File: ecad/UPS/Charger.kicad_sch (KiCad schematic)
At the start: 70 parts, among them J1 Barrel_Jack, J2 Conn_01x02_Pin, J5 Conn_01x02_Pin, J6 Conn_01x02_Pin, Q1 CSD18540Q5B, Q2 Q_PMOS_DGS, Q4 Q_PMOS_DGS, Q5 CSD18540Q5B, Q6 CSD18540Q5B, Q7 CSD18540Q5B, U1 BQ25730RSNR

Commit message: Started GND consolidation
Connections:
- net GND: now also C1.2, C2.2, C28.1, C29.1, C30.1, C31.1, C38.2, R1.2, R2.2, R3.2
- net GNDA: no longer C1.2, C2.2, C28.1, C29.1, C30.1, C31.1, C38.2, R1.2, R2.2, R3.2
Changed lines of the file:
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@@
 	(global_label "REGN"
 		(shape input)
-		(at 257.81 152.4 90)
+		(at 257.81 152.4 0)
 		(fields_autoplaced yes)
 		(effects
@@
 		)
 		(property "Intersheetrefs" "${INTERSHEET_REFS}"
-			(at 257.81 144.3953 90)
+			(at 265.8147 152.4 0)
 			(hide yes)
 			(show_name no)
@@
 			)
 		)
-		(property "Value" "GNDA"
-			(at 146.05 242.5699 90)
+		(property "Value" "GND"
+			(at 148.59 238.76 90)
 			(show_name no)
 			(do_not_autoplace no)
@@
 					(size 1.27 1.27)
 				)
-				(justify right)
 			)
 		)
@@
 			)
 		)
-		(property "Value" "GNDA"
+		(property "Value" "GND"
 			(at 102.87 163.8299 90)
 			(show_name no)
@@
 			)
 		)
-		(property "Value" "GNDA"
-			(at 260.35 201.93 0)
+		(property "Value" "GND"
+			(at 262.89 198.1199 0)
 			(show_name no)
 			(do_not_autoplace no)
@@
 					(size 1.27 1.27)
 				)
+				(justify left)
 			)
 		)
@@
 			)
 		)
-		(property "Value" "GNDA"
-			(at 243.84 203.2 0)
+		(property "Value" "GND"
+			(at 246.38 199.3899 0)
 			(show_name no)
 			(do_not_autoplace no)
@@
 					(size 1.27 1.27)
 				)
+				(justify left)
 			)
 		)
@@
 			)
 		)
-		(property "Value" "GNDA"
-			(at 102.87 177.7999 90)
+		(property "Value" "GND"
+			(at 105.41 173.99 90)
 			(show_name no)
 			(do_not_autoplace no)
@@
 					(size 1.27 1.27)
 				)
-				(justify right)
 			)
 		)
@@
 			)
 		)
-		(property "Value" "GNDA"
-			(at 250.19 201.93 0)
+		(property "Value" "GND"
+			(at 252.73 198.1199 0)
 			(show_name no)
 			(do_not_autoplace no)
@@
 					(size 1.27 1.27)
 				)
+				(justify left)
 			)
 		)
@@
 			)
 		)
-		(property "Value" "GNDA"
+		(property "Value" "GND"
 			(at 273.05 203.2 0)
 			(show_name no)

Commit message: Rename all grounds to GND
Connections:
- net GND: now also C68.2, C69.2, C70.2, J2.2 (Pin_2), J5.2 (Pin_2), J6.2 (Pin_2)
- net GNDA: no longer C68.2, C69.2, C70.2, J2.2 (Pin_2), J5.2 (Pin_2), J6.2 (Pin_2)

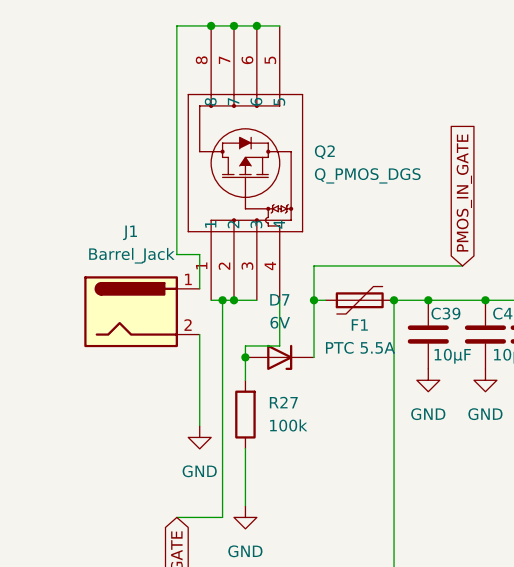
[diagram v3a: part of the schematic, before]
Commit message: Little routing, also fixed barrel jack to match input
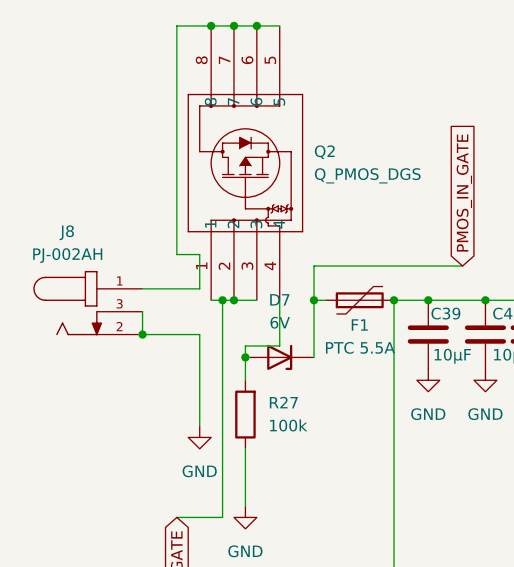
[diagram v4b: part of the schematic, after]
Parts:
- removed J1: Barrel_Jack, Connector_BarrelJack:BarrelJack_Horizontal, symbol Connector:Barrel_Jack
- added J8: PJ-002AH, PJ-002AH:CUI_PJ-002AH, symbol PJ-002AH:PJ-002AH
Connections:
- net GND: now also J8.2, J8.3
- net at Q2.5, Q2.6, Q2.7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: now also J8.1
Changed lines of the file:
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@@
 	)
 	(junction
+		(at 92.71 87.63)
+		(diameter 0)
+		(color 0 0 0 0)
+	)
+	(junction
 		(at 321.31 95.25)
 		(diameter 0)
@@
 	(wire
 		(pts
+			(xy 92.71 85.09) (xy 92.71 87.63)
+		)
+		(stroke
+			(width 0)
+			(type default)
+		)
+	)
+	(wire
+		(pts
 			(xy 104.14 90.17) (xy 104.14 92.71)
 		)
@@
 	(wire
 		(pts
+			(xy 92.71 87.63) (xy 99.06 87.63)
+		)
+		(stroke
+			(width 0)
+			(type default)
+		)
+	)
+	(wire
+		(pts
 			(xy 273.05 177.8) (xy 273.05 185.42)
 		)
@@
 	(wire
 		(pts
+			(xy 92.71 82.55) (xy 99.06 82.55)
+		)
+		(stroke
+			(width 0)
+			(type default)
+		)
+	)
+	(wire
+		(pts
 			(xy 101.6 83.82) (xy 102.87 83.82)
 		)
@@
 	)
 	(symbol
+		(lib_id "PJ-002AH:PJ-002AH")
+		(at 87.63 85.09 0)
+		(unit 1)
+		(body_style 1)
+		(exclude_from_sim no)
+		(in_bom yes)
+		(on_board yes)
+		(in_pos_files yes)
+		(dnp no)
+		(fields_autoplaced yes)
+		(property "Reference" "J8"
+			(at 84.3943 76.2 0)
+			(show_name no)
+			(do_not_autoplace no)
+			(effects
+				(font
+					(size 1.27 1.27)
+				)
+			)
+		)
+		(property "Value" "PJ-002AH"
+			(at 84.3943 78.74 0)
+			(show_name no)
+			(do_not_autoplace no)
+			(effects
+				(font
+					(size 1.27 1.27)
+				)
+			)
+		)
+		(property "Footprint" "PJ-002AH:CUI_PJ-002AH"
+			(at 87.63 85.09 0)
+			(hide yes)
+			(show_name no)
+			(do_not_autoplace no)
+			(effects
+				(font
+					(size 1.27 1.27)
+				)
+				(justify bottom)
+			)
+		)
+		(property "Datasheet" ""
+			(at 87.63 85.09 0)
+			(hide yes)
+			(show_name no)
+			(do_not_autoplace no)
+			(effects
+				(font
+					(size 1.27 1.27)
+				)
+			)
+		)
+		(property "Description" "Power Barrel Connector Jack 2.10mm ID (0.083), 5.50mm OD (0.217) Through Hole, Right Angle"
+			(at 87.63 85.09 0)
+			(hide yes)
+			(show_name no)
+			(do_not_autoplace no)
+			(effects
+				(font
+					(size 1.27 1.27)
+				)
+				(justify bottom)
+			)
+		)
+		(property "MF" "Same Sky"
+			(at 87.63 85.09 0)
+			(hide yes)
+			(show_name no)
+			(do_not_autoplace no)
+			(effects
+				(font
+					(size 1.27 1.27)
+				)
+				(justify bottom)
+			)
+		)
+		(property "Package" "None"
+			(at 87.63 85.09 0)
+			(hide yes)
+			(show_name no)
+			(do_not_autoplace no)
+			(effects
+				(font
+					(size 1.27 1.27)
+				)
+				(justify bottom)
+			)
+		)
+		(property "Price" "None"
+			(at 87.63 85.09 0)
+			(hide yes)
+			(show_name no)
+			(do_not_autoplace no)
+			(effects
+				(font
+					(size 1.27 1.27)
+				)
+				(justify bottom)
+			)
+		)
+		(property "Check_prices" "https://www.snapeda.com/parts/PJ-002AH/Same+Sky/view-part/?ref=eda"
+			(at 87.63 85.09 0)
+			(hide yes)
+			(show_name no)
+			(do_not_autoplace no)
+			(effects
+				(font
+					(size 1.27 1.27)
+				)
+				(justify bottom)
+			)
+		)
+		(property "STANDARD" "Manufacturer recommendations"
+			(at 87.63 85.09 0)
+			(hide yes)
+			(show_name no)
+			(do_not_autoplace no)
+			(effects
+				(font
+					(size 1.27 1.27)
+				)
+				(justify bottom)
+			)
+		)
+		(property "SnapEDA_Link" "https://www.snapeda.com/parts/PJ-002AH/Same+Sky/view-part/?ref=snap"
+			(at 87.63 85.09 0)
+			(hide yes)
+			(show_name no)
+			(do_not_autoplace no)
+			(effects
+				(font
+					(size 1.27 1.27)
+				)
+				(justify bottom)
+			)
+		)
+		(property "MP" "PJ-002AH"
+			(at 87.63 85.09 0)
+			(hide yes)
+			(show_name no)
+			(do_not_autoplace no)
+			(effects
+				(font
+					(size 1.27 1.27)
+				)
+				(justify bottom)
+			)
+		)
+		(property "Purchase-URL" "https://www.snapeda.com/api/url_track_click_mouser/?unipart_id=448876&manufacturer=Same Sky&part_name=PJ-002AH&search_term=pj-002ah"
+			(at 87.63 85.09 0)
+			(hide yes)
+			(show_name no)
+			(do_not_autoplace no)
+			(effects
+				(font
+					(size 1.27 1.27)
+				)
+				(justify bottom)
+			)
+		)
+		(property "Availability" "In Stock"
+			(at 87.63 85.09 0)
+			(hide yes)
+			(show_name no)
+			(do_not_autoplace no)
+			(effects
+				(font
+					(size 1.27 1.27)
+				)
+				(justify bottom)
+			)
+		)
+		(property "MANUFACTURER" "CUI INC"
+			(at 87.63 85.09 0)
+			(hide yes)
+			(show_name no)
+			(do_not_autoplace no)
+			(effects
+				(font
+					(size 1.27 1.27)
+				)
+				(justify bottom)
+			)
+		)
+		(pin "1"
+		)
+		(pin "2"
+		)
+		(pin "3"
+		)
+		(instances
+			(project "UPS"
+				(path "/9d92b60a-4a6b-449c-b462-cab19e69d38c/58e8621a-e50a-4c31-8927-fd6b72ccb3ce"
+					(reference "J8")
+					(unit 1)
+				)
+			)
+		)
+	)
+	(symbol
 		(lib_id "Device:C")
 		(at 330.2 88.9 0)
@@
 					(unit 1)
 				)
-			)
-		)
-	)
-	(symbol
-		(lib_id "Connector:Barrel_Jack")
-		(at 91.44 85.09 0)
-		(unit 1)
-		(body_style 1)
-		(exclude_from_sim no)
-		(in_bom yes)
-		(on_board yes)
-		(in_pos_files yes)
-		(dnp no)
-		(fields_autoplaced yes)
-		(property "Reference" "J1"
-			(at 91.44 76.2 0)
-			(show_name no)
-			(do_not_autoplace no)
-			(effects
-				(font
-					(size 1.27 1.27)
-				)
-			)
-		)
-		(property "Value" "Barrel_Jack"
-			(at 91.44 78.74 0)
-			(show_name no)
-			(do_not_autoplace no)
-			(effects
-				(font
-					(size 1.27 1.27)
-				)
-			)
-		)
-		(property "Footprint" "Connector_BarrelJack:BarrelJack_Horizontal"
-			(at 92.71 86.106 0)
-			(hide yes)
-			(show_name no)
-			(do_not_autoplace no)
-			(effects
-				(font
-					(size 1.27 1.27)
-				)
-			)
-		)
-		(property "Datasheet" ""
-			(at 92.71 86.106 0)
-			(hide yes)
-			(show_name no)
-			(do_not_autoplace no)
-			(effects
-				(font
-					(size 1.27 1.27)
-				)
-			)
-		)
-		(property "Description" "DC Barrel Jack"
-			(at 91.44 85.09 0)
-			(hide yes)
-			(show_name no)
-			(do_not_autoplace no)
-			(effects
-				(font
-					(size 1.27 1.27)
-				)
-			)
-		)
-		(pin "1"
-		)
-		(pin "2"
-		)
-		(instances
-			(project "Charger"
-				(path "/58c05fa3-b10b-4b83-957c-b8220bb8f680"
-					(reference "J1")
-					(unit 1)
-				)
-			)
-			(project "UPS"
-				(path "/9d92b60a-4a6b-449c-b462-cab19e69d38c/58e8621a-e50a-4c31-8927-fd6b72ccb3ce"
-					(reference "J1")
-					(unit 1)
-				)

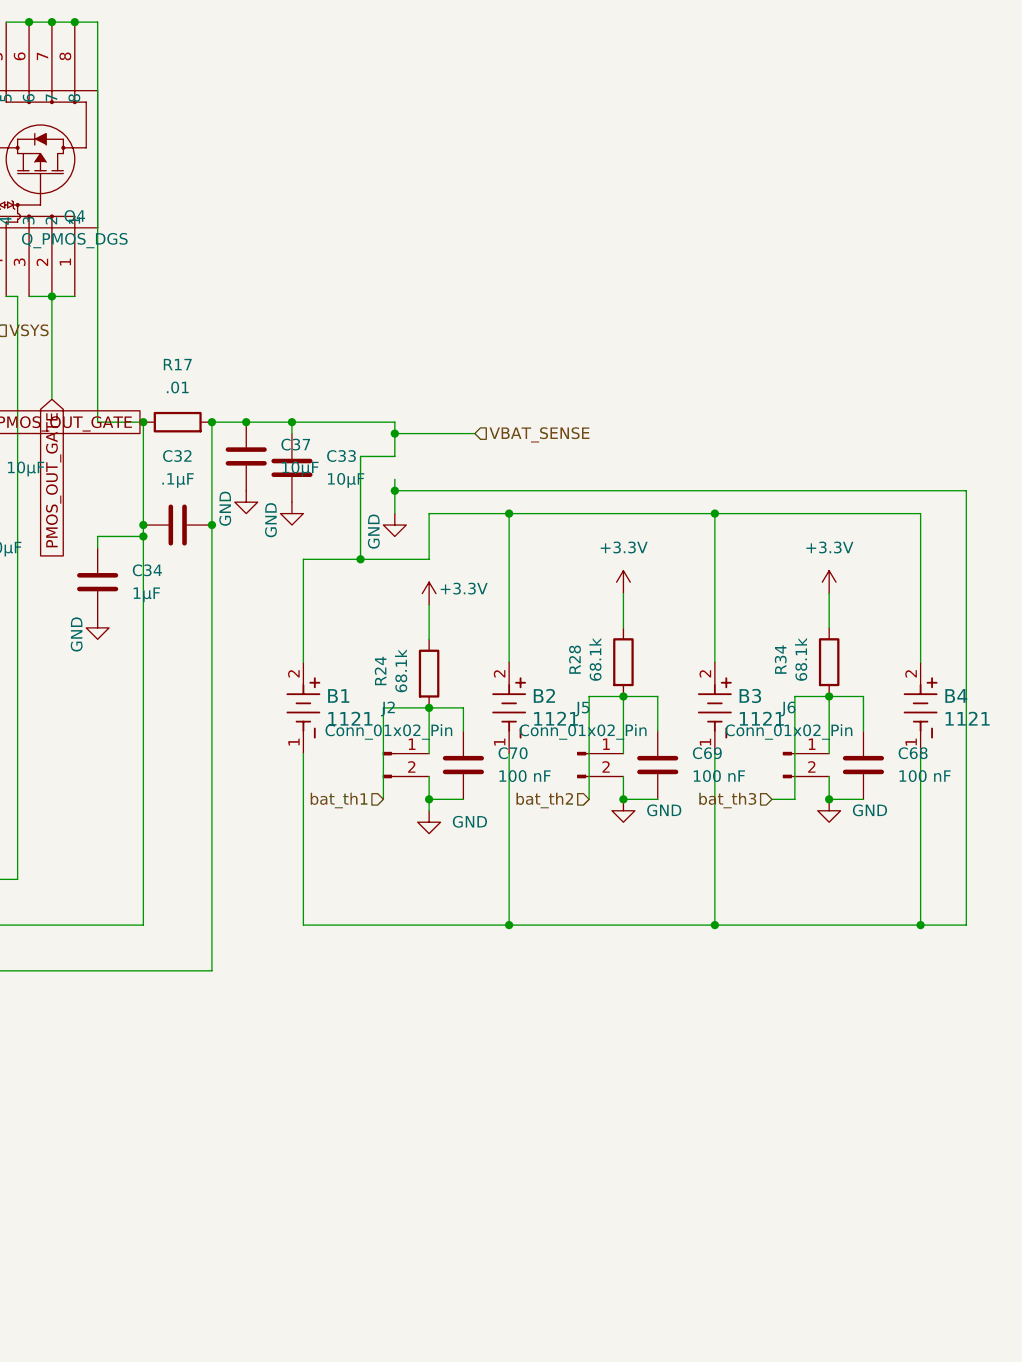
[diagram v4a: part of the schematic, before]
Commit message: touches
Add battery and board thermistor circuits on PC0/PC1.

Implement ADC sampling, temperature conversion, and sensor fault reporting.

Enable the STM32 ADC drivers and poll temperatures in the main loop.

Add the OLED connector on PB10/PB11 and update PCB footprints and net assignments.

Add a Raspberry Pi mounting-hole footprint.

Exclude local docs and test folders from Git.

five ADC sensor inputs

fan-control logic.
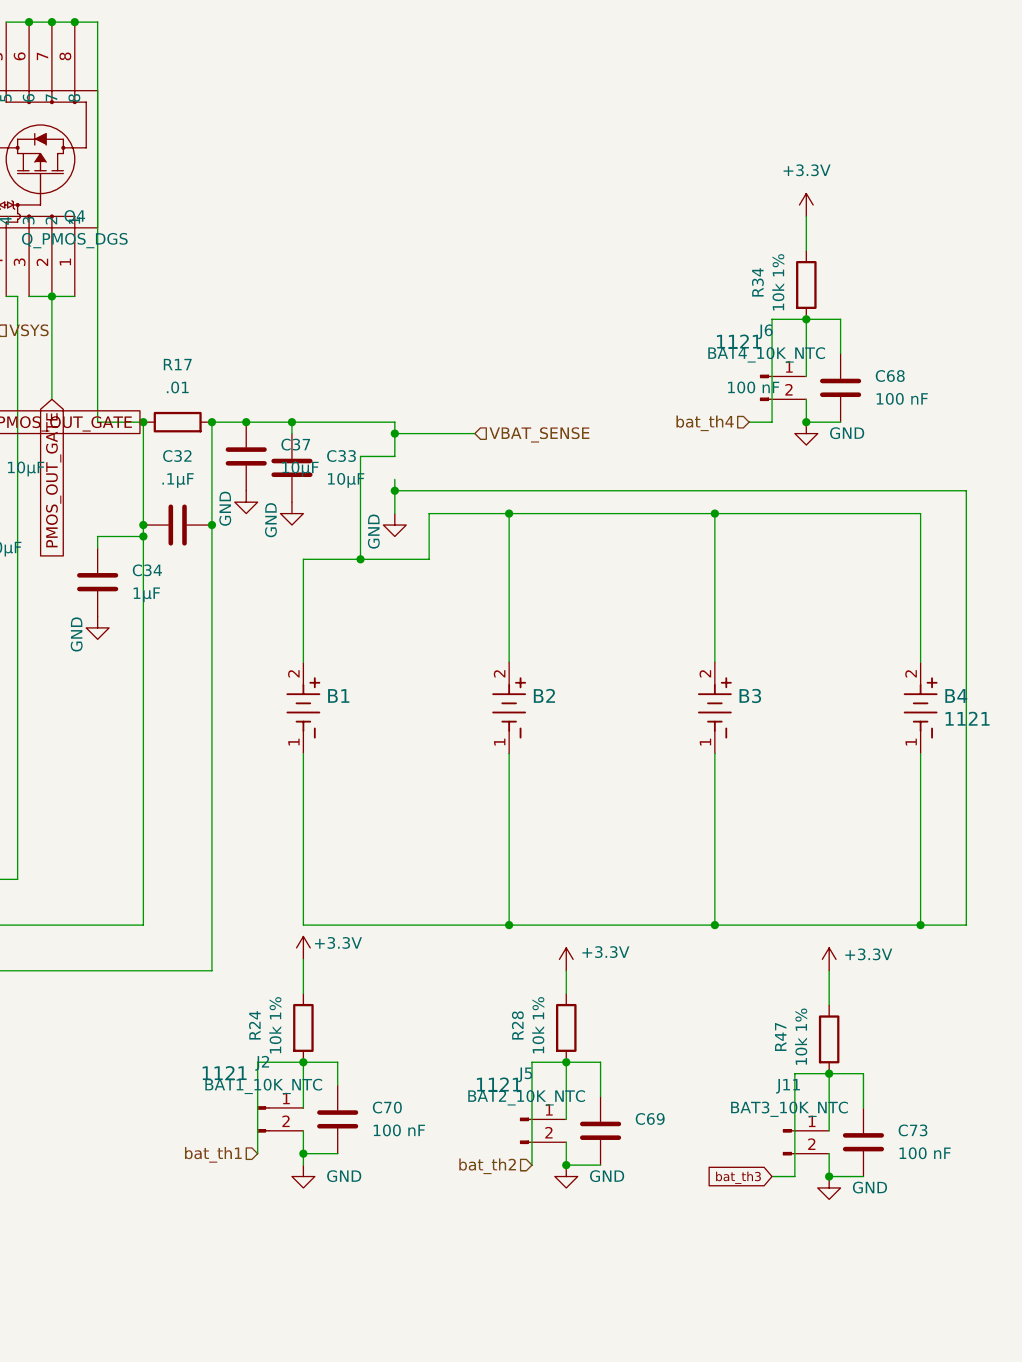
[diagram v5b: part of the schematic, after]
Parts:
- added C73: 100 nF, Capacitor_SMD:C_0603_1608Metric, symbol Device:C
- added J11: BAT3_10K_NTC, Connector_JST:JST_XH_B2B-XH-A_1x02_P2.50mm_Vertical, symbol Connector:Conn_01x02_Pin
- added R47: 10k 1%, Resistor_SMD:R_0805_2012Metric_Pad1.20x1.40mm_HandSolder, symbol Device:R
- J2: value Conn_01x02_Pin -> BAT1_10K_NTC
- J5: value Conn_01x02_Pin -> BAT2_10K_NTC
- J6: value Conn_01x02_Pin -> BAT4_10K_NTC
- R24, R28, R34: value 68.1k -> 10k 1%
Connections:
- net +3.3V: now also R47.1
- net GND: now also C73.2, J11.2 (Pin_2)
- net bat_th3: now also C73.1, J11.1 (Pin_1), R47.2; no longer C68.1, J6.1 (Pin_1), R34.2
- new net bat_th4: C68.1, J6.1 (Pin_1), R34.2
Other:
- moved on the sheet: C68, C69, C70, J2, J5, J6, R24, R28, R34

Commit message: Organize UPS placement for Pi 5 mounting and power-stage review
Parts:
- C39, C40, C41, C42, C43, C44: footprint Capacitor_SMD:C_0603_1608Metric -> Capacitor_SMD:C_1210_3225Metric
- C51, C52, C53, C54, C55, C56, C57: footprint Capacitor_SMD:C_0603_1608Metric -> Capacitor_SMD:C_0805_2012Metric
- U1: footprint UPS:RSN0032B-IPC_C -> Package_DFN_QFN:Texas_RSN_WQFN-32-1EP_4x4mm_P0.4mm_EP2.8x2.8mm
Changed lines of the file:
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@@
 			)
 		)
-		(property "Footprint" "Capacitor_SMD:C_0603_1608Metric"
+		(property "Footprint" "Capacitor_SMD:C_0805_2012Metric"
 			(at 293.0652 100.33 0)
 			(hide yes)
@@
 			)
 		)
-		(property "Footprint" "Capacitor_SMD:C_0603_1608Metric"
+		(property "Footprint" "Capacitor_SMD:C_0805_2012Metric"
 			(at 285.4452 91.44 0)
 			(hide yes)
@@
 			)
 		)
-		(property "Footprint" "Capacitor_SMD:C_0603_1608Metric"
+		(property "Footprint" "Capacitor_SMD:C_0805_2012Metric"
 			(at 290.5252 91.44 0)
 			(hide yes)
@@
 			)
 		)
-		(property "Footprint" "Capacitor_SMD:C_0603_1608Metric"
+		(property "Footprint" "Capacitor_SMD:C_1210_3225Metric"
 			(at 125.4252 91.44 0)
 			(hide yes)
@@
 			)
 		)
-		(property "Footprint" "Capacitor_SMD:C_0603_1608Metric"
+		(property "Footprint" "Capacitor_SMD:C_0805_2012Metric"
 			(at 295.6052 91.44 0)
 			(hide yes)
@@
 			)
 		)
-		(property "Footprint" "Capacitor_SMD:C_0603_1608Metric"
+		(property "Footprint" "Capacitor_SMD:C_0805_2012Metric"
 			(at 281.6352 100.33 0)
 			(hide yes)
@@
 			)
 		)
-		(property "Footprint" "Capacitor_SMD:C_0603_1608Metric"
+		(property "Footprint" "Capacitor_SMD:C_0805_2012Metric"
 			(at 280.3652 91.44 0)
 			(hide yes)
@@
 			)
 		)
-		(property "Footprint" "Capacitor_SMD:C_0603_1608Metric"
+		(property "Footprint" "Capacitor_SMD:C_1210_3225Metric"
 			(at 136.8552 91.44 0)
 			(hide yes)
@@
 			)
 		)
-		(property "Footprint" "Capacitor_SMD:C_0603_1608Metric"
+		(property "Footprint" "Capacitor_SMD:C_1210_3225Metric"
 			(at 147.0152 91.44 0)
 			(hide yes)
@@
 			)
 		)
-		(property "Footprint" "Capacitor_SMD:C_0603_1608Metric"
+		(property "Footprint" "Capacitor_SMD:C_0805_2012Metric"
 			(at 287.9852 100.33 0)
 			(hide yes)
@@
 			)
 		)
-		(property "Footprint" "Capacitor_SMD:C_0603_1608Metric"
+		(property "Footprint" "Capacitor_SMD:C_1210_3225Metric"
 			(at 152.0952 91.44 0)
 			(hide yes)
@@
 			)
 		)
-		(property "Footprint" "Capacitor_SMD:C_0603_1608Metric"
+		(property "Footprint" "Capacitor_SMD:C_1210_3225Metric"
 			(at 141.9352 91.44 0)
 			(hide yes)
@@
 			)
 		)
-		(property "Footprint" "Capacitor_SMD:C_0603_1608Metric"
+		(property "Footprint" "Capacitor_SMD:C_1210_3225Metric"
 			(at 131.7752 91.44 0)
 			(hide yes)
@@
 			)
 		)
-		(property "Footprint" "UPS:RSN0032B-IPC_C"
+		(property "Footprint" "Package_DFN_QFN:Texas_RSN_WQFN-32-1EP_4x4mm_P0.4mm_EP2.8x2.8mm"
 			(at 185.42 104.14 0)
 			(hide yes)

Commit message: bazinga
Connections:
- net GND: no longer Q7.4, U1.31 (HIDRV1)
- new net: Q7.4, U1.31 (HIDRV1)
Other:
- note added: "TODO (Tyler): review removed #PWR015 GND symbol and add it back at the correct node. Removed from HIDRV1/Q7 gate at (177.8,119.38), 90 deg; confirm connection before restoring. C13 pin 2 still shares HIDRV1; review its input-filter return wiring."
- moved on the sheet: C13, C14, C15

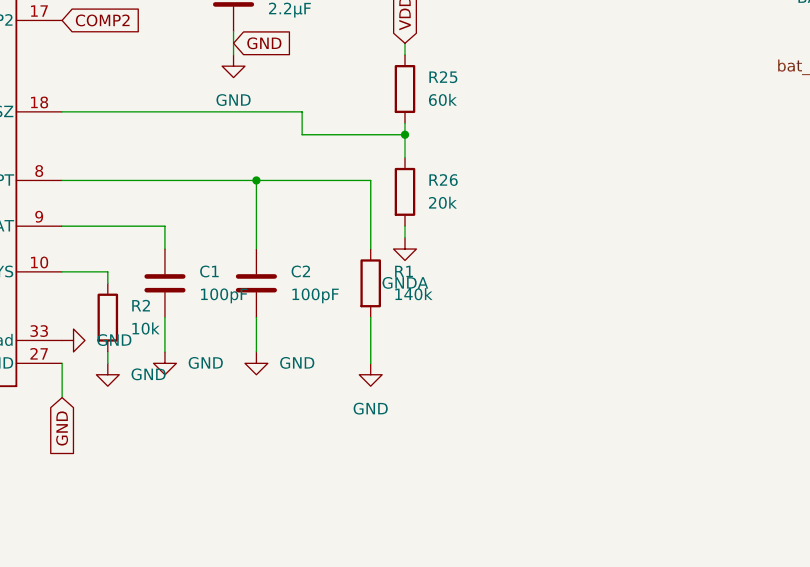
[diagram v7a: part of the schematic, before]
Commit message: eh
Grounded the charger’s cell-count divider.
Corrected C9 from 470 pF to 470 nF.
Connected the STM’s unused LCD supply pin.
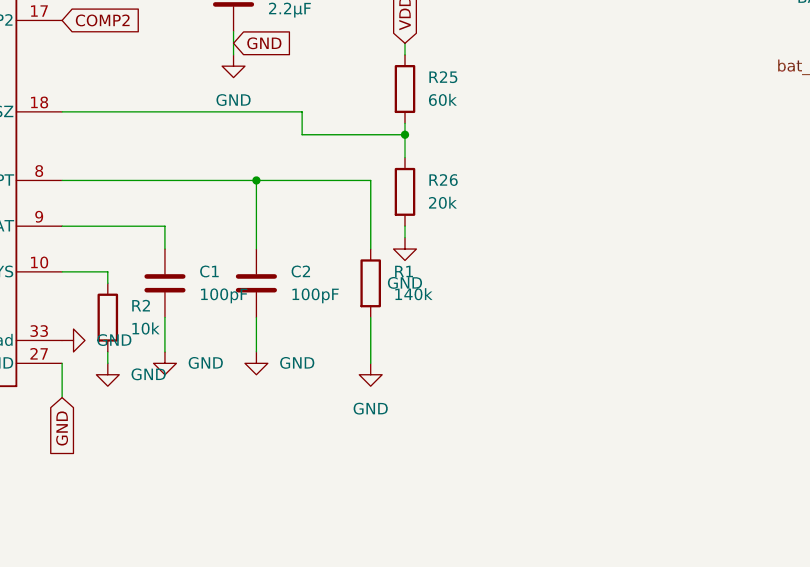
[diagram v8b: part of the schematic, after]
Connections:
- net GNDA is gone; now on net GND: R26.2
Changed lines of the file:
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@@
 			)
 		)
-		(property "Value" "GNDA"
+		(property "Value" "GND"
 			(at 276.86 189.23 0)
 			(show_name no)
